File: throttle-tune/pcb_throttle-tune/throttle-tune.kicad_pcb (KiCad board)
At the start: 2 copper layers, 48 parts, among them IC1 ATMEGA8A-P, J1 Screw_Terminal_01x03, J10 9V supply / small battery, J2 Screw_Terminal_01x03, J3 Screw_Terminal_01x03, J4 Screw_Terminal_01x03, J5 Conn_01x03_Pin, J6 UART, J7 gpio-reserve, J8 gpio-reserve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

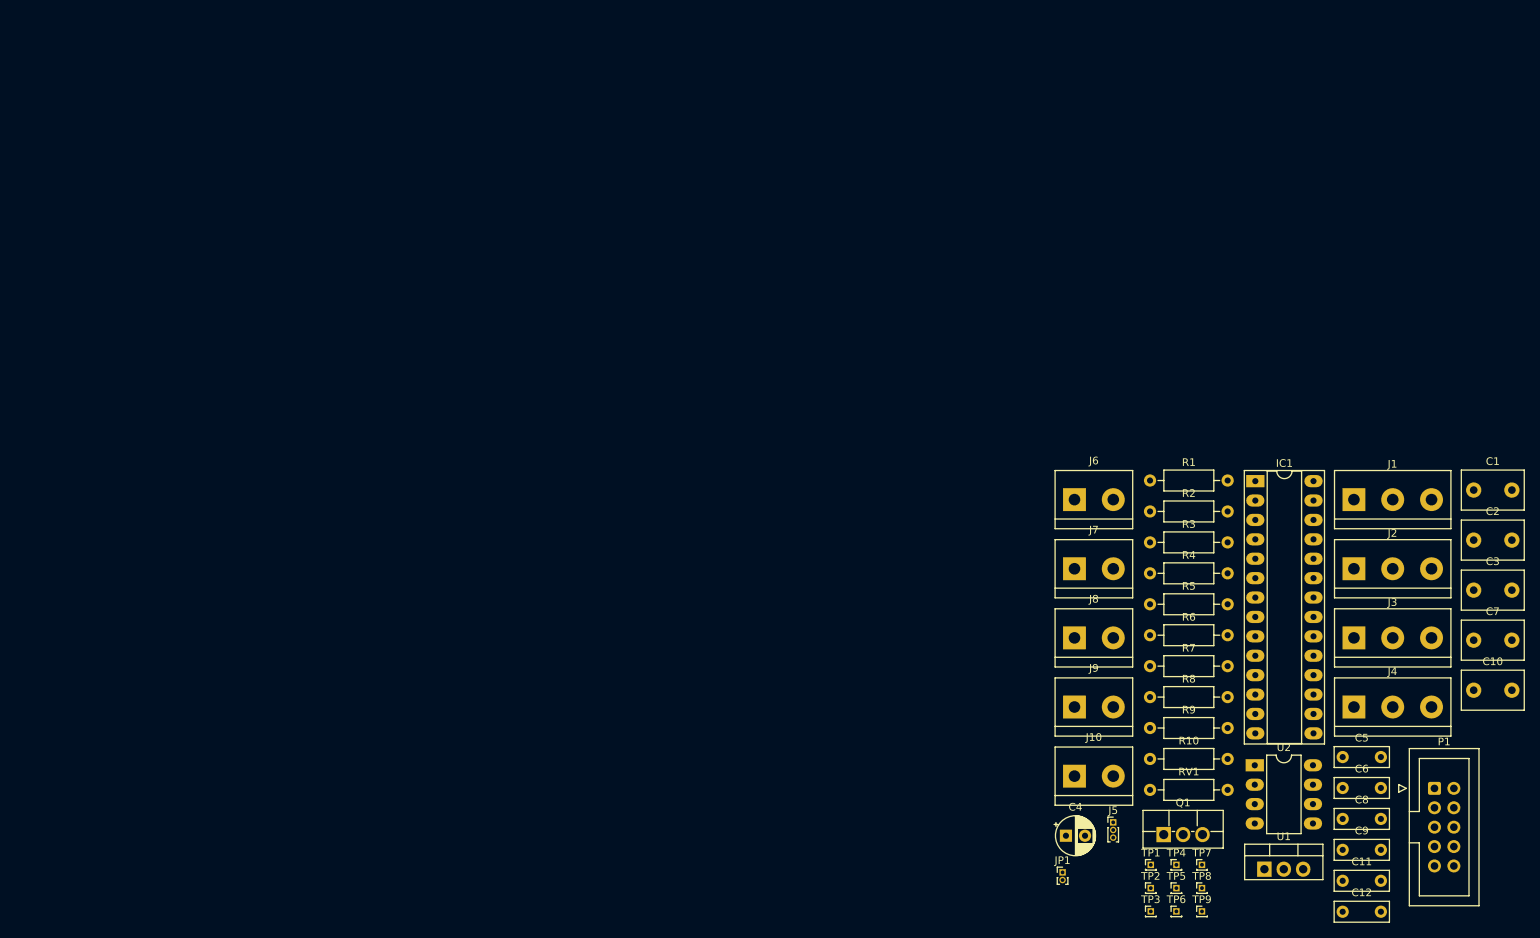
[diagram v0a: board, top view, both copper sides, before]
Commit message: pcb: arrange components
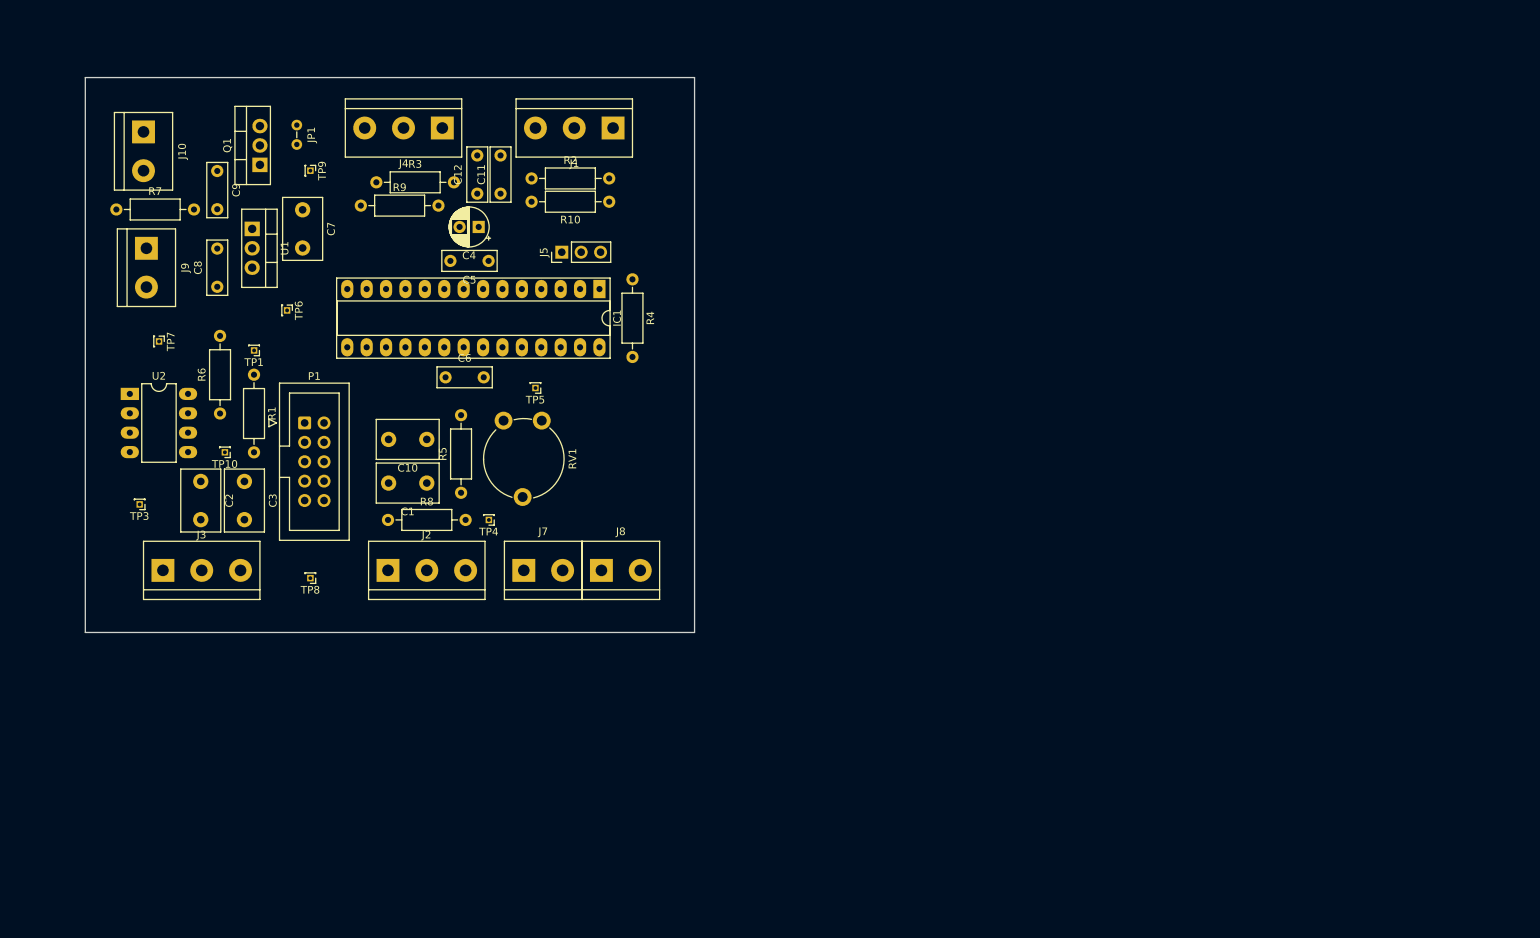
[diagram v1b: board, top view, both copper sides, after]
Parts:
- removed J6: UART, TerminalBlock:TerminalBlock_bornier-2_P5.08mm
- removed TP2: TestPoint, Connector_PinHeader_1.00mm:PinHeader_1x01_P1.00mm_Vertical
- added TP10: DAC, Connector_PinHeader_1.00mm:PinHeader_1x01_P1.00mm_Vertical, F.Cu at (27.4, 57.2)
- J1: value Screw_Terminal_01x03 -> 3speedSw-in
- J2: value Screw_Terminal_01x03 -> gas-pedal-in
- J3: value Screw_Terminal_01x03 -> throttle-out
- J4: value Screw_Terminal_01x03 -> 3speedSw-out
- J5: footprint Connector_PinHeader_1.00mm:PinHeader_1x03_P1.00mm_Vertical -> Connector_PinHeader_2.54mm:PinHeader_1x03_P2.54mm_Vertical
- J9: value Screw_Terminal_01x02 -> 5V/GND
- JP1: footprint Connector_PinHeader_1.00mm:PinHeader_1x02_P1.00mm_Vertical -> Jumper_AKL:Jumper_P2.54mm_D0.7mm
- Q1: footprint Package_TO_SOT_THT:TO-220F-3_Vertical -> Package_TO_SOT_THT:TO-220-3_Vertical
- RV1: footprint Resistor_THT:R_Axial_DIN0207_L6.3mm_D2.5mm_P10.16mm_Horizontal -> Potentiometer_THT:Potentiometer_Piher_PT-10-V10_Vertical
- TP1: value TestPoint -> PWM
- TP3: value TestPoint -> Throttle-Out
- TP7: value TestPoint -> GND
- TP8: value TestPoint -> 5V controller
- TP9: value TestPoint -> 9V
- moved C9 172.1 mm to (26.4, 20.4), turned to -90 degrees
- moved C2 166.8 mm to (24.3, 61.0), turned to -90 degrees
- moved C7 163.3 mm to (37.6, 25.4), turned to -90 degrees
- moved C8 163.0 mm to (26.4, 35.5), turned to 90 degrees
- moved C3 161.6 mm to (30.0, 61.0), turned to -90 degrees
- moved U1 156.8 mm to (31.0, 27.9), turned to -90 degrees
- moved J3 156.2 mm to (19.3, 72.6)
- moved P1 155.5 mm to (37.9, 53.3)
- moved U2 155.1 mm to (15.0, 49.5)
- moved TP7 152.8 mm to (18.8, 42.7), turned to -90 degrees
- moved TP9 151.7 mm to (38.6, 20.3), turned to -90 degrees
- moved J10 148.2 mm to (16.8, 15.2), turned to -90 degrees
- moved R7 147.9 mm to (13.2, 25.4)
- moved Q1 147.3 mm to (32.0, 19.6), turned to 90 degrees
- moved C12 147.2 mm to (60.5, 23.3), turned to 90 degrees
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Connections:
- IC1 pad 23: /Throttle-IN-Filtered -> /Throttle-OUT
- IC1 pad 24: /Throttle-OUT -> /Throttle-IN-Filtered
- IC1 pad 4: /speedSwitch2_fast -> /speedSwitch1_slow
- IC1 pad 5: /speedSwitch1_slow -> /speedSwitch2_fast
- J1 pad 3: +5V_motorcontroller -> Net-(J1-Pin_3)
- J10 pad 1: GND -> 9V-Batt
- J10 pad 2: 9V-Batt -> GND
- J3 pad 1: +5V_motorcontroller -> GND
- J3 pad 3: GND -> +5V_motorcontroller
- J4 pad 1: +5V_motorcontroller -> Net-(J1-Pin_1)
- J4 pad 3: Net-(J1-Pin_1) -> Net-(J1-Pin_3)
- J9 pad 1: +5V -> GND
- J9 pad 2: GND -> +5V
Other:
- board outline added: 79.8 x 72.6 mm

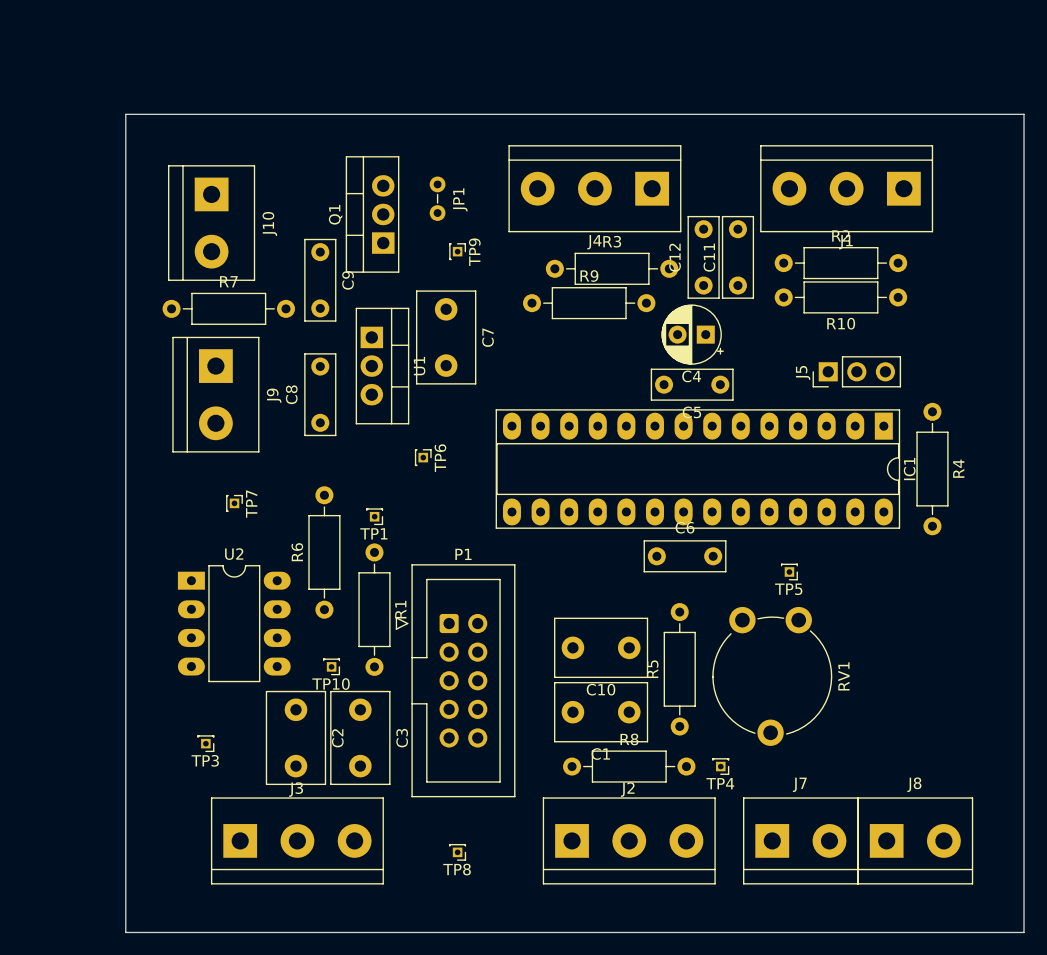
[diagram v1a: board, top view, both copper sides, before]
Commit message: pcb: finish layout, pcb2gcode, adj pins - milled pcb
milled pcb and populated, works well but
error with P-channel mosfet (missing NPN driver)
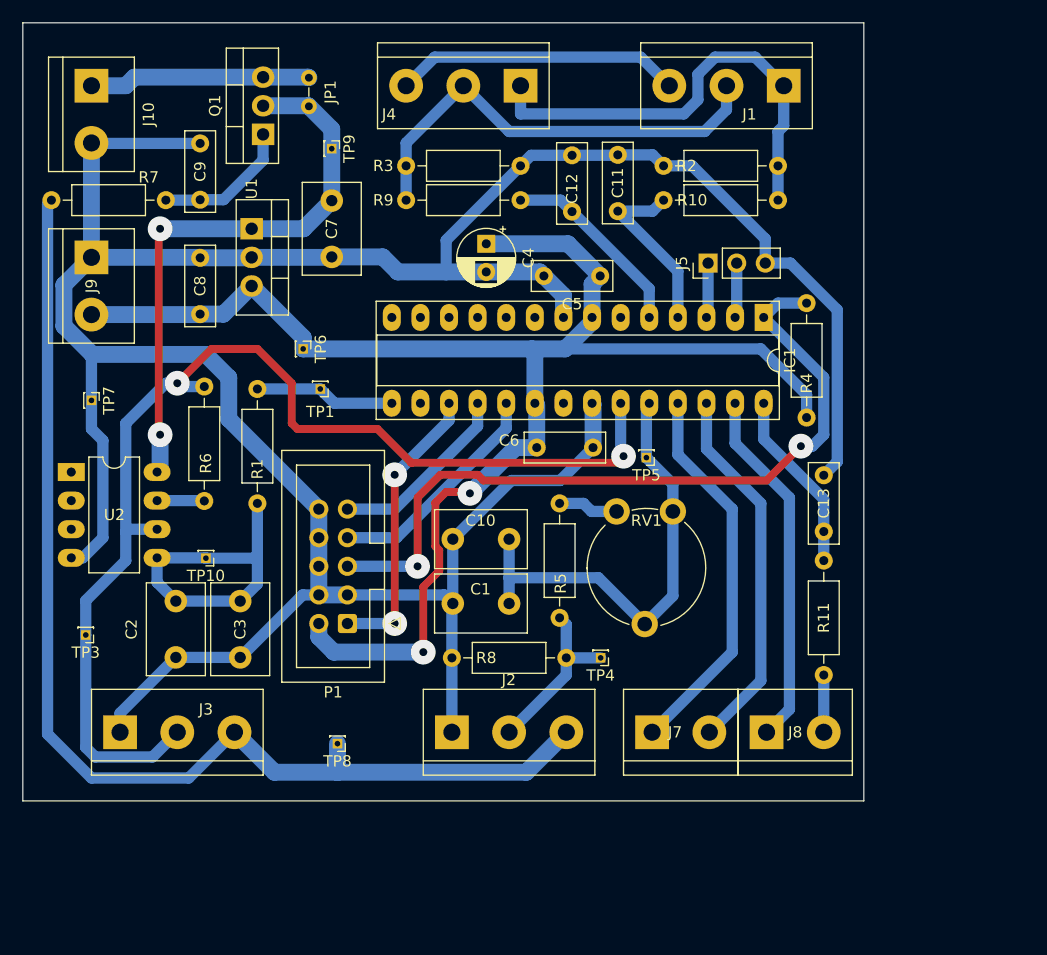
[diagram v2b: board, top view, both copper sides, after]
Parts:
- added C13: 100nF, Capacitor_THT:C_Disc_D7.0mm_W2.5mm_P5.00mm, F.Cu at (71.1, 45.2)
- added R11: 100k, Resistor_THT:R_Axial_DIN0207_L6.3mm_D2.5mm_P10.16mm_Horizontal, F.Cu at (71.1, 57.9)
- J5: value Conn_01x03_Pin -> UART [TX, RX, GND]
- J8: value gpio-reserve -> reserve, reverse-sw
- R7: value 470 -> 1k
- TP6: value TestPoint -> 5V
- U1: value LM7805_TO220 -> LM7805
- moved C4 21.1 mm to (41.1, 19.6), turned to -90 degrees
- moved R1 17.9 mm to (20.8, 32.5)
- moved TP5 16.3 mm to (55.4, 38.6)
- moved R3 16.1 mm to (34.0, 12.7)
- moved TP7 15.6 mm to (6.10, 33.5)
- moved JP1 14.8 mm to (25.4, 4.88)
- moved J4 14.8 mm to (44.2, 5.59)
- moved R4 14.8 mm to (69.6, 24.9)
- moved RV1 14.8 mm to (52.7, 43.4)
- moved TP10 14.8 mm to (16.3, 47.5)
- moved J9 14.7 mm to (6.10, 20.8)
- moved R9 14.4 mm to (34.0, 15.7)
- moved TP9 14.4 mm to (27.4, 11.2)
- moved C8 14.4 mm to (15.7, 25.9)
- moved J2 14.4 mm to (38.1, 63.0)
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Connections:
- IC1 pad 28: Net-(IC1-(ADC5/SCL)PC5) -> /Reverse-sw
- J8 pad 2: Net-(IC1-(ADC5/SCL)PC5) -> /REV-in
- P1 pad 3: unconnected-(P1-Pad3) -> GND
- P1 pad 4: unconnected-(P1-Pad4) -> GND
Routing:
- net GND: track 0.00 -> 267.4 mm
- net +5V: track 0.00 -> 135.3 mm, vias 0 -> 2
- net /Throttle-OUT: track 0.00 -> 103.9 mm, vias 0 -> 2
- net +5V_motorcontroller: track 0.00 -> 102.4 mm
- net /RESET: track 0.00 -> 68.1 mm, vias 0 -> 2
- net +9V: track 0.00 -> 51.4 mm, vias 0 -> 2
- net /Throttle-IN-Filtered: track 0.00 -> 41.2 mm
- net Net-(J1-Pin_1): track 0.00 -> 40.7 mm
- net Net-(J1-Pin_2): track 0.00 -> 40.2 mm
- net Net-(IC1-(ADC2)PC2): track 0.00 -> 34.2 mm
- net Net-(IC1-(ADC3)PC3): track 0.00 -> 33.1 mm
- net Net-(IC1-(ADC4/SDA)PC4): track 0.00 -> 32.1 mm
- net Net-(U2B-+): track 0.00 -> 28.6 mm
- net /MOSI: track 0.00 -> 25.8 mm, vias 0 -> 2
- net Net-(J1-Pin_3): track 0.00 -> 25.5 mm
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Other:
- board size 79.8 x 72.6 mm -> 74.7 x 69.1 mm

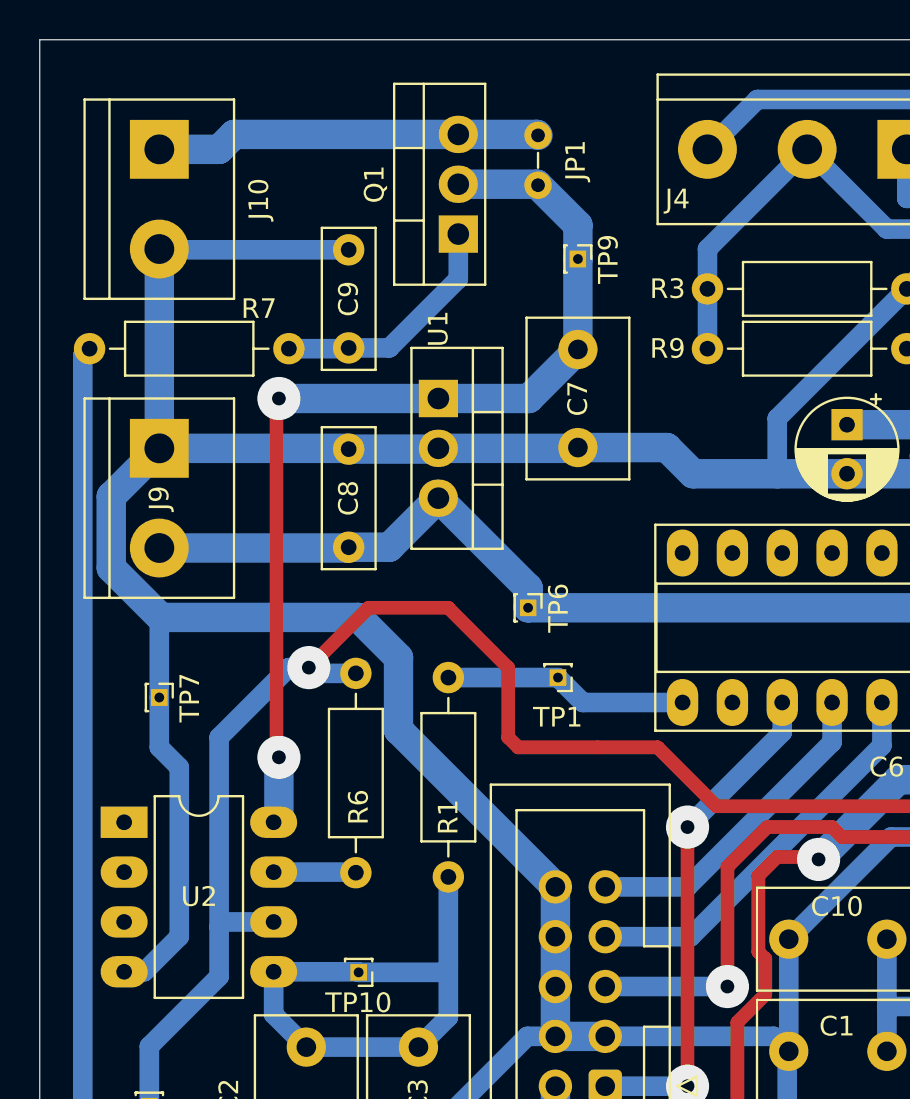
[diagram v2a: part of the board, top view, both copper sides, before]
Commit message: pcb: fix supply cutoff (add NPN), update layout
Note: fixed in already milled pcb by adding transistor with wires
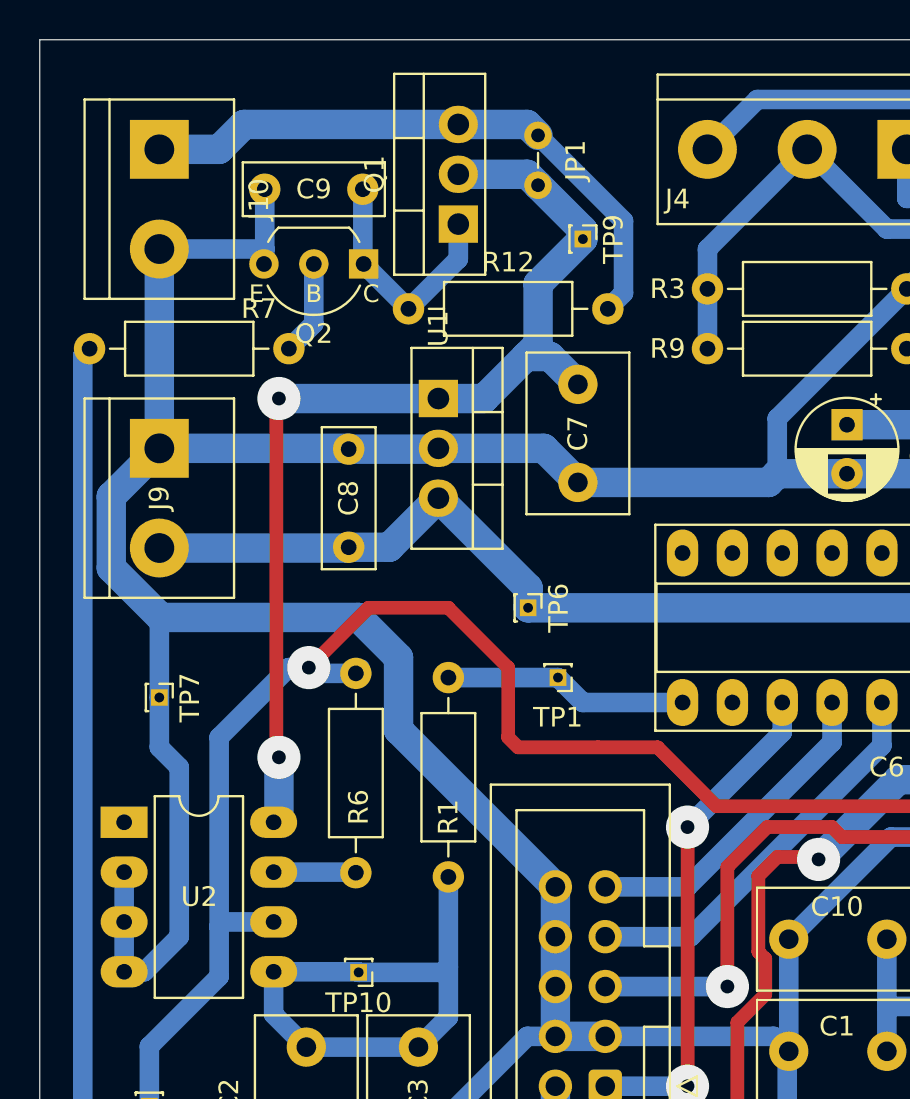
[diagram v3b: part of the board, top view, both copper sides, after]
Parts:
- added Q2: BC547, Package_TO_SOT_THT_AKL:TO-92_Inline_Wide_CBE, F.Cu at (16.5, 11.4)
- added R12: 47k, Resistor_THT:R_Axial_DIN0207_L6.3mm_D2.5mm_P10.16mm_Horizontal, F.Cu at (18.8, 13.7)
- R10, R11, R9: value 100k -> 220k
- R2, R3: value 4k7 -> 5k6
- R5, R8: value 2k2 -> 3k9
- R6: value 1k -> 330
- R7: value 1k -> 22k
- moved C9 8.12 mm to (16.5, 7.62), turned to 180 degrees
- moved C7 1.78 mm to (27.4, 17.6)
- moved TP9 1.05 mm to (27.7, 10.2)
- moved Q1 0.51 mm to (21.3, 9.40)
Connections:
- R7 pad 2: Net-(Q1-G) -> Net-(Q2-B)
- U2 pad 2: unconnected-(U2A---Pad2) -> GND
- U2 pad 3: unconnected-(U2A-+-Pad3) -> GND
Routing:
- net 9V-Batt: track 19.6 -> 31.0 mm
- net GND: track 267.4 -> 272.4 mm
- net Net-(Q2-B): track 0.00 -> 4.84 mm
- net +9V: track 51.4 -> 53.7 mm
